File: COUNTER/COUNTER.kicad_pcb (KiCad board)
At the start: 2 copper layers, 76.1 x 64.6 mm, 28 parts, among them J1 Conn_01x08, J10 Conn_01x04, J2 Conn_01x03, J3 Conn_01x08, U46 74LS161, U47 74LS245, U48 74LS161

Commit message: Updating Counter
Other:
- board text added: "+VCC"
- board text added: "-GND"
- board text added: "74LS245"
- board text added: "BCD DECADE COUNTER"
- board text added: "theWickedWebDev/8-bit-computer"
- board text added: "w/ jump"
- board text removed: "+ VCC"
- board text removed: "-Gnd"
- board text removed: "theWickedWebDev"
- board text removed: "w/ Jump"

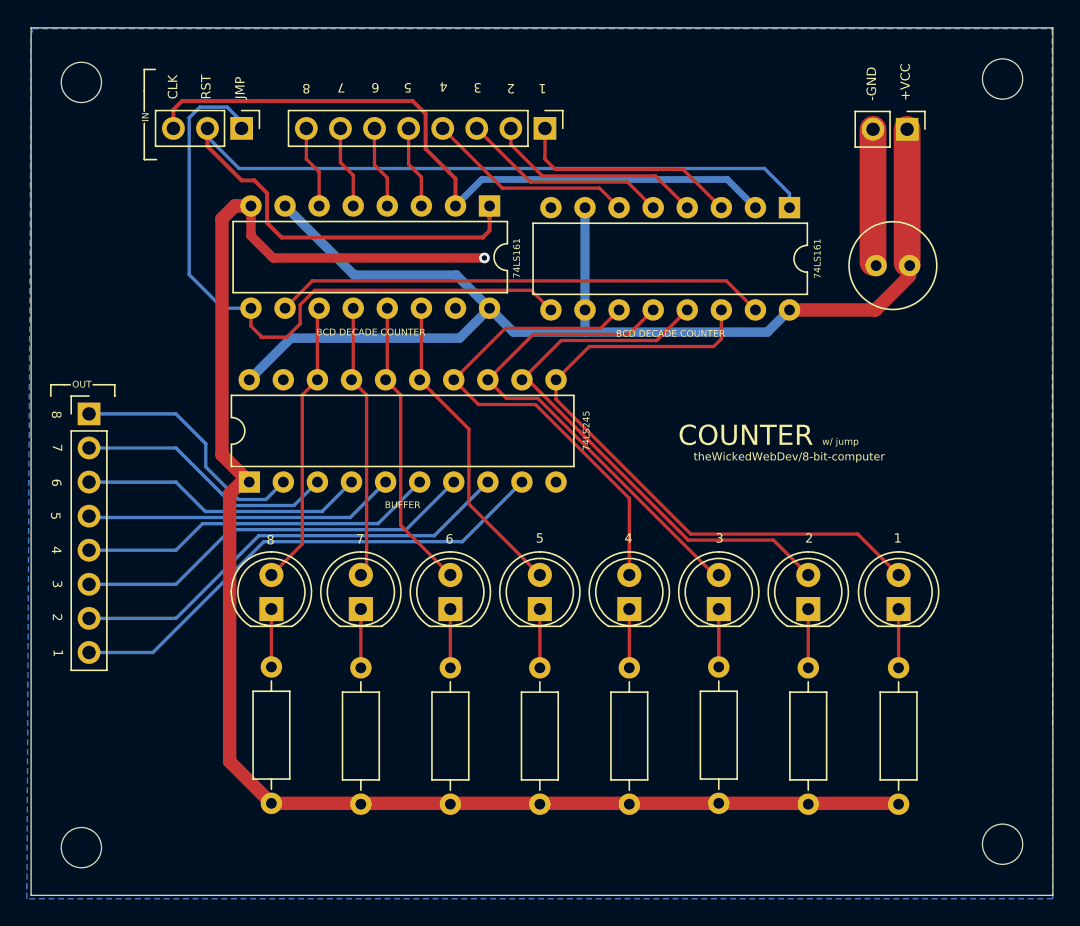
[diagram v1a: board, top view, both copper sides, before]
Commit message: More Additions, Counter, ALU, Clock
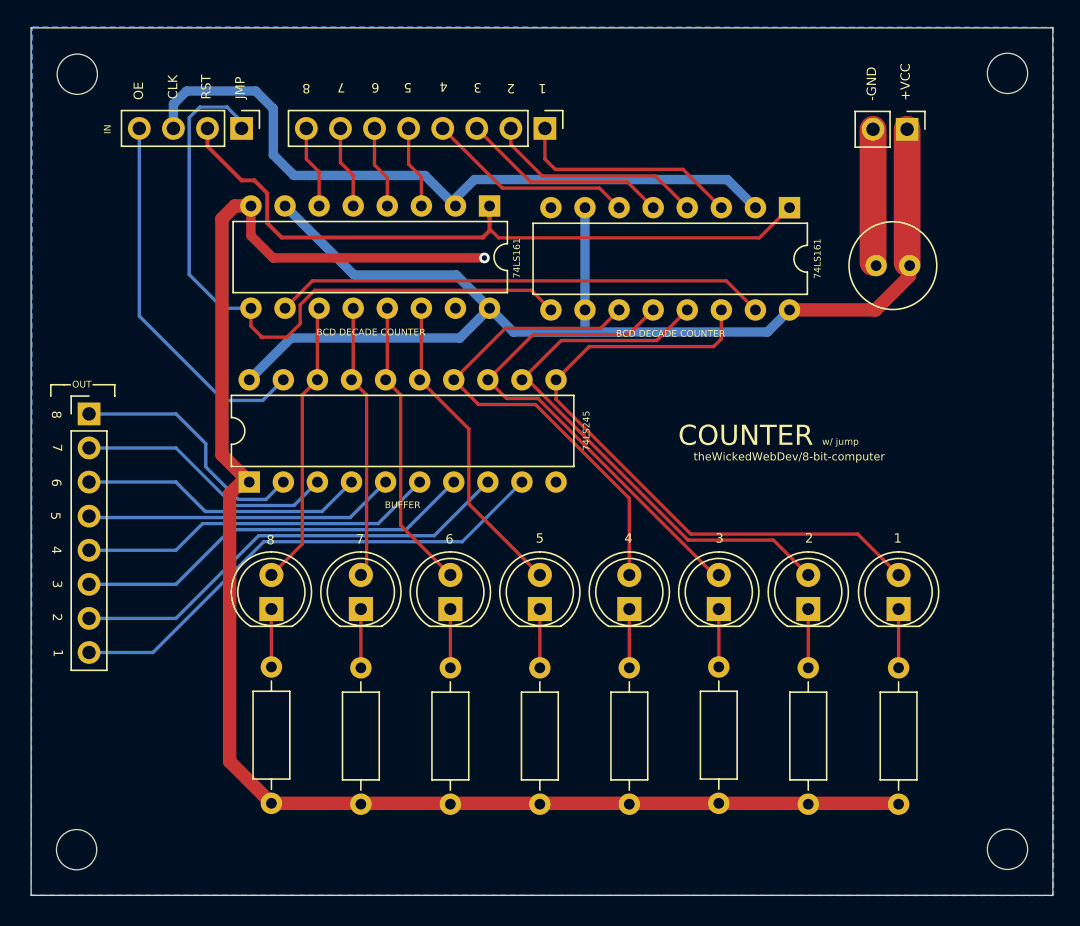
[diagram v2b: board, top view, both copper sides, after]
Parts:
- J2: value Conn_01x03 -> Conn_01x04; footprint Connector_PinHeader_2.54mm:PinHeader_1x03_P2.54mm_Vertical -> Connector_PinHeader_2.54mm:PinHeader_1x04_P2.54mm_Vertical
- moved REF** 0.68 mm to (74.9, 32.5)
- moved REF** 0.56 mm to (144.3, 32.5)
- moved REF** 0.53 mm to (144.3, 90.3)
- moved REF** 0.39 mm to (74.9, 90.3)
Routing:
- net /OE: track 0.00 -> 28.0 mm
- net /RESET: track 76.6 -> 55.7 mm
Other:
- board text added: "OE"

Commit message: Updating components
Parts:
- removed D44, D45, D46, D47, D48, D49, D50, D51: LED, LED_THT:LED_D5.0mm
- removed R11, R12, R13, R14, R15, R16, R17, R18: R_US, Resistor_THT:R_Axial_DIN0207_L6.3mm_D2.5mm_P10.16mm_Horizontal
- removed the REF** at (74.9, 90.3)
- removed the REF** at (74.9, 32.5)
- removed the REF** at (144.3, 90.3)
- removed the REF** at (144.3, 32.5)
- added BAR1: HDSP-4830_2, Display:HDSP-4830, F.Cu at (139.9, 55.9)
- added J1: Screw_Terminal_01x02, TerminalBlock_Phoenix:TerminalBlock_Phoenix_MKDS-1,5-2_1x02_P5.00mm_Horizontal, F.Cu at (140.5, 49.0)
- added REF**: MountingHole_3mm_Pad_Via, MountingHole:MountingHole_3mm_Pad_Via, F.Cu at (142.5, 73.0)
- added REF**: MountingHole_3mm_Pad_Via, MountingHole:MountingHole_3mm_Pad_Via, F.Cu at (80.2, 73.0)
- added REF**: MountingHole_3mm_Pad_Via, MountingHole:MountingHole_3mm_Pad_Via, F.Cu at (142.5, 34.6)
- added REF**: MountingHole_3mm_Pad_Via, MountingHole:MountingHole_3mm_Pad_Via, F.Cu at (80.2, 34.5)
- added RN1: R_Network08, Resistor_THT:R_Array_SIP9, F.Cu at (137.0, 70.5)
- J22: renamed from J2; value Conn_01x04 -> Conn_01x05; footprint Connector_PinHeader_2.54mm:PinHeader_1x04_P2.54mm_Vertical -> Connector_PinHeader_2.54mm:PinHeader_1x05_P2.54mm_Vertical
- moved J22 11.1 mm to (98.3, 36.8)
- moved J23 11.1 mm to (120.9, 36.8)
- moved C10 10.7 mm to (133.7, 36.6), turned to 0 degrees
- moved J10 8.25 mm to (128.5, 36.7)
- moved J24 7.45 mm to (81.2, 62.9), turned to 180 degrees
- moved U14 0.92 mm to (128.9, 42.5)
- renumbered C8 to C10, J3 to J23, J1 to J24, U46 to U12, U48 to U14
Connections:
- net /CLOCK renamed CLOCK
- net /D1 renamed D1
- net /D2 renamed D2
- net /D3 renamed D3
- net /D4 renamed D4
- net /D5 renamed D5
- net /D6 renamed D6
- net /D7 renamed D7
- net /D8 renamed D8
- net /JUMP renamed JUMP
- net /OE renamed OE
- net /RESET renamed RESET
- net /Y1 renamed Y1
- net /Y2 renamed Y2
- net /Y3 renamed Y3
- net /Y4 renamed Y4
- net /Y5 renamed Y5
- net /Y6 renamed Y6
- net /Y7 renamed Y7
- net /Y8 renamed Y8
- J10 pad 1: VCC -> GND
- J10 pad 2: GND -> VCC
- U14 pad 10: VCC -> CE
- U14 pad 7: VCC -> CE
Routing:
- net GND: track 126.5 -> 0.00 mm, vias 1 -> 0
- net VCC: track 92.6 -> 0.00 mm
- net CE: track 0.00 -> 37.6 mm
- net RESET: track 55.7 -> 37.3 mm
- net Net-(BAR1-Pad7): track 20.6 -> 37.0 mm
- net Net-(BAR1-Pad8): track 21.3 -> 37.0 mm
- net Net-(BAR1-Pad6): track 21.9 -> 37.0 mm
- net Net-(BAR1-Pad1): track 48.1 -> 34.4 mm
- net Net-(BAR1-Pad5): track 23.6 -> 37.0 mm
- net D1: track 16.9 -> 6.90 mm
- net D2: track 16.3 -> 6.90 mm
- net Net-(BAR1-Pad19): track 0.00 -> 9.22 mm
- net Net-(BAR1-Pad18): track 0.00 -> 9.22 mm
- net Net-(BAR1-Pad16): track 0.00 -> 9.22 mm
- net Net-(BAR1-Pad14): track 0.00 -> 9.22 mm
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- added copper zone on In2.Cu, net VCC
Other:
- board size 76.1 x 64.6 mm -> 69.1 x 45.3 mm
- copper layers 2 -> 4
- board text added: "+"
- board text added: "-"
- board text added: "BCD Decade Counter"
- board text added: "CE"
- board text added: "NC"
- board text removed: "BCD DECADE COUNTER"
